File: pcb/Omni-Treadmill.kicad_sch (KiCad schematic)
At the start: 1 part

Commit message: updated schematic
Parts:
- removed D1: 1N4001, Diode_THT:D_DO-41_SOD81_P10.16mm_Horizontal, symbol Diode:1N4001
- added U1, U6: IR2110PBF, PG-DIP-14-1_INF, symbol customs:IR2110PBF
- added U2, U3, U4, U5: IRFP250PBF, TO-247AC_VIS, symbol customs:IRFP250PBF

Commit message: uh
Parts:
- removed U4: IRFP250PBF, TO-247AC_VIS, symbol customs:IRFP250PBF
- removed U6: IR2110PBF, PG-DIP-14-1_INF, symbol customs:IR2110PBF
- added C1: C, symbol Device:C
- added D1, D2: 1N914, Diode_THT:D_DO-35_SOD27_P7.62mm_Horizontal, symbol Diode:1N914
- added R1, R2, R3, R4: R, symbol Device:R
- added U4: IR2110PBF, PG-DIP-14-1_INF, symbol customs:IR2110PBF
- added U6: IRFP250PBF, TO-247AC_VIS, symbol customs:IRFP250PBF
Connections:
- net at U5.1 (G): now also R3.2
- net at U1.1 (LO): now also D1.1 (K), R1.1
- net GND: now reaches U1.2 (COM)
- net GND: now also U4.2 (COM)
- net at U1.5 (VS): now also C1.2
- net at U1.6 (VB): now also C1.1
- net at U1.7 (HO): now also D2.1 (K), R2.1
- net at U3.1 (G): now also D2.2 (A), R2.2
- net at U2.1 (G): now also D1.2 (A), R1.2
- new net: R3.1, U4.7 (HO)
- new net: R4.2, U6.1 (G)
- new net: R4.1, U4.1 (LO)
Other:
- moved on the sheet: U1, U2, U3

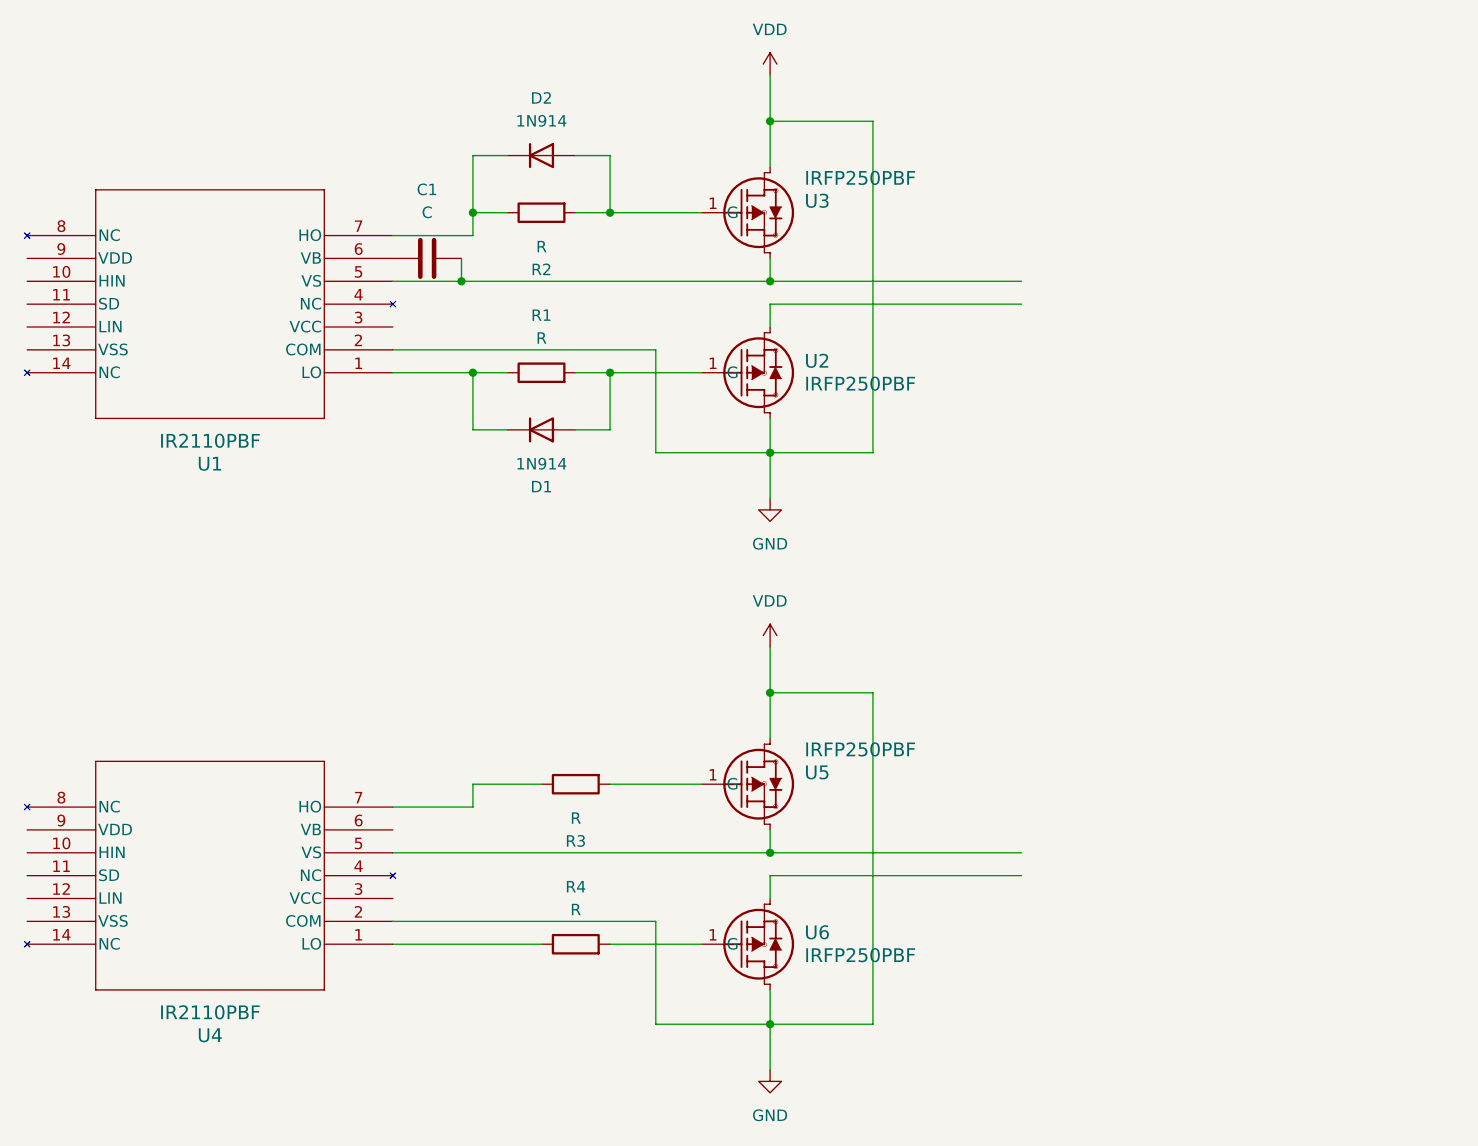
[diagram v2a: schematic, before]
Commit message: updated hbridge and components
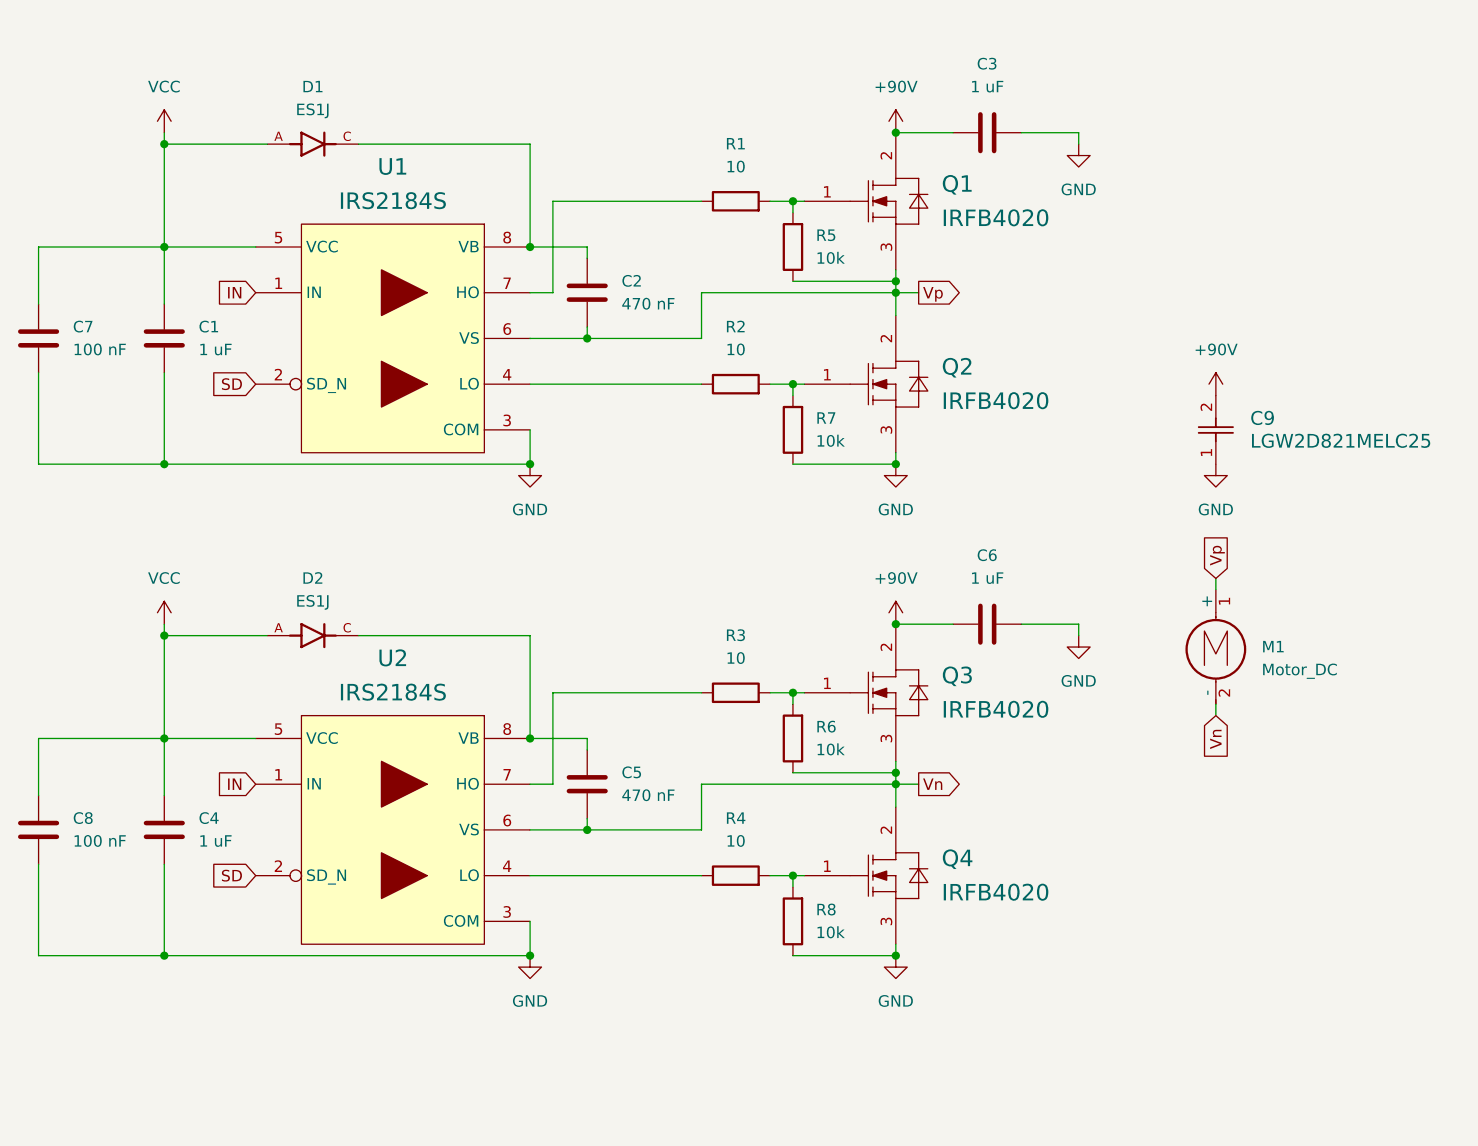
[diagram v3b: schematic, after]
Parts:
- removed D1, D2: 1N914, Diode_THT:D_DO-35_SOD27_P7.62mm_Horizontal, symbol Diode:1N914
- removed U1, U4: IR2110PBF, PG-DIP-14-1_INF, symbol customs:IR2110PBF
- removed U2, U3, U5, U6: IRFP250PBF, TO-247AC_VIS, symbol customs:IRFP250PBF
- added C2, C5: 470 nF, Capacitor_SMD:C_1812_4532Metric_Pad1.57x3.40mm_HandSolder, symbol Device:C
- added C3, C4, C6: 1 uF, Capacitor_SMD:C_1812_4532Metric_Pad1.57x3.40mm_HandSolder, symbol Device:C
- added C7, C8: 100 nF, Capacitor_SMD:C_1206_3216Metric_Pad1.33x1.80mm_HandSolder, symbol Device:C
- added C9: LGW2D821MELC25, CAP_C25_NCH, symbol 2026-03-09_22-13-50:LGW2D821MELC25
- added D1, D2: ES1J, Library:DIOM4325X250N, symbol 2026-03-09_22-13-50:ES1J
- added M1: Motor_DC, symbol Motor:Motor_DC
- added Q1, Q2, Q3, Q4: IRFB4020, Library:IFX-PG-TO220-3-904, symbol IRFB4020:IRFB4020
- added R5, R6, R7, R8: 10k, Resistor_SMD:R_0805_2012Metric_Pad1.20x1.40mm_HandSolder, symbol Device:R
- added U1, U2: IRS2184S, Library:SOIC127P600X175-8N-12-V, symbol IRS2184S:IRS2184S
- C1: value C -> 1 uF; footprint (none) -> Capacitor_SMD:C_1812_4532Metric_Pad1.57x3.40mm_HandSolder
- R1, R2, R3, R4: value R -> 10; footprint (none) -> Resistor_SMD:R_1206_3216Metric_Pad1.30x1.75mm_HandSolder
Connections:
- net GND: now also C1.1, C3.2, C4.1, C6.2, C7.2, C8.2, C9.1, Q2.3 (SOURCE), Q4.3 (SOURCE), R7.1, R8.1, U1.3 (COM), U2.3 (COM)
- net at R2.1: now also U1.4 (LO)
- net at R2.2: now also Q2.1 (GATE), R7.2
- net at R3.1: now also U2.7 (HO)
- net at R3.2: now also Q3.1 (GATE), R6.2
- net at R4.2: now also Q4.1 (GATE), R8.2
- net at R1.1: now also U1.7 (HO)
- net at R1.2: now also Q1.1 (GATE), R5.2
- net VCC: now reaches C1.2
- net VCC: now also C4.2, C7.1, C8.1, D1.A, D2.A, U1.5 (VCC), U2.5 (VCC)
- net at R4.1: now also U2.4 (LO)
- new net: C5.1, D2.C, U2.8 (VB)
- new net: C2.1, D1.C, U1.8 (VB)
- new net +90V: C3.1, C6.1, C9.2, Q1.2 (DRAIN), Q3.2 (DRAIN)
- new net IN: U1.1 (IN), U2.1 (IN)
- new net SD: U1.2 (SD_N), U2.2 (SD_N)
- new net Vn: C5.2, M1.2 (-), Q3.3 (SOURCE), Q4.2 (DRAIN), R6.1, U2.6 (VS)
- new net Vp: C2.2, M1.1 (+), Q1.3 (SOURCE), Q2.2 (DRAIN), R5.1, U1.6 (VS)
